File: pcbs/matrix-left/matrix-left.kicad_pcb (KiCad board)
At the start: 2 copper layers, 51 parts, among them J4 Conn_01x11, SW1 SW_Push, SW10 SW_Push, SW11 SW_Push, SW12 SW_Push, SW13 SW_Push, SW14 SW_Push, SW15 SW_Push, SW16 SW_Push, SW17 SW_Push, SW18 SW_Push, SW19 SW_Push, SW2 SW_Push, SW20 SW_Push, SW21 SW_Push, SW22 SW_Push, SW23 SW_Push, SW24 SW_Push, SW25 SW_Push, SW3 SW_Push, SW4 SW_Push, SW5 SW_Push, SW6 SW_Push, SW7 SW_Push, SW8 SW_Push, SW9 SW_Push

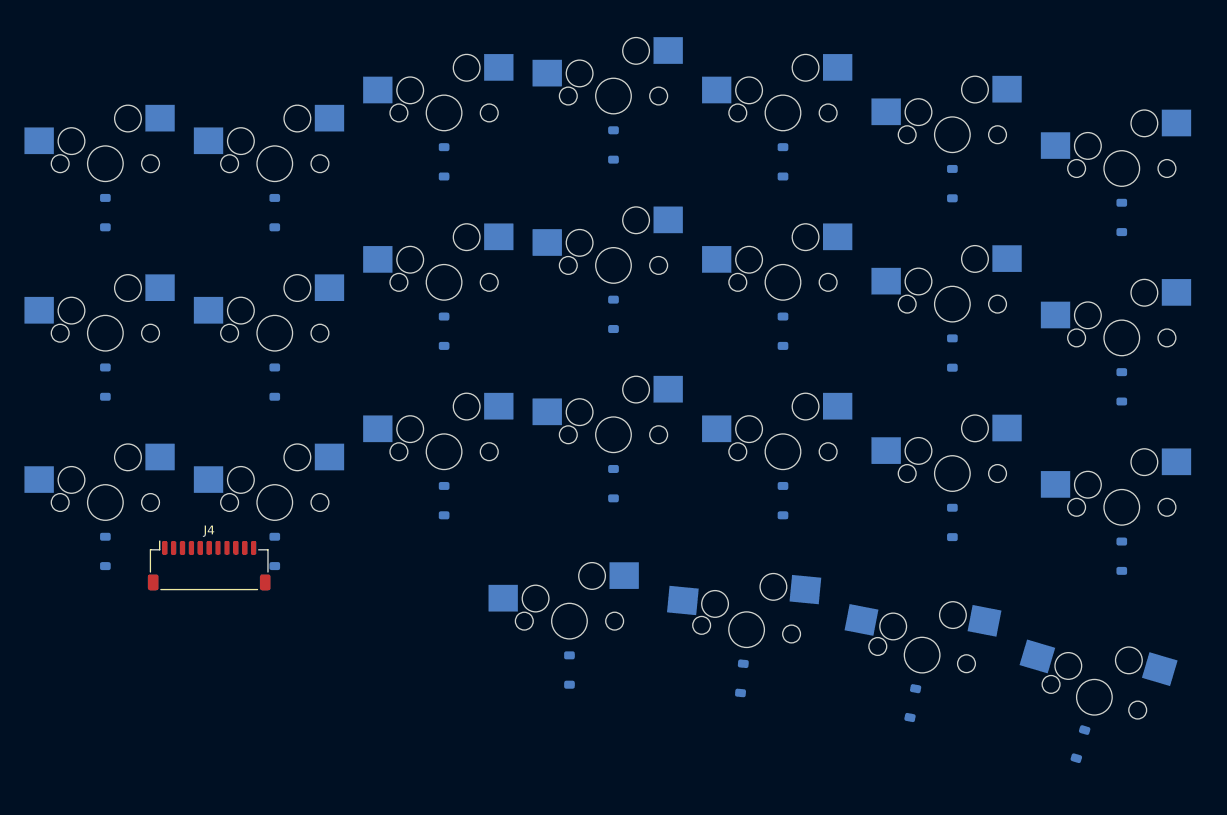
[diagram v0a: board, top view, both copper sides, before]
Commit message: Flip rows R1-R3 on the matrix board and place its J1
All keys in R1-R3 (thumb keys included) are now rotated 180 degrees, so
their hot-swap sockets sit in the front half of the key. R0 keeps its
orientation, which leaves a socket-free band between R0 and R1 across
the board where the column traces can run sideways to J1 at the R0C3 /
R1C3 boundary; below R1 every row gap keeps the usual socket-to-diode
arrangement.

The KiCad board is updated by running place_matrix.py: switches and
diodes placed, diodes on the back, and J1 on the back below R0C3.

Co-Authored-By: Claude Opus 5.5 <noreply@anthropic.com>
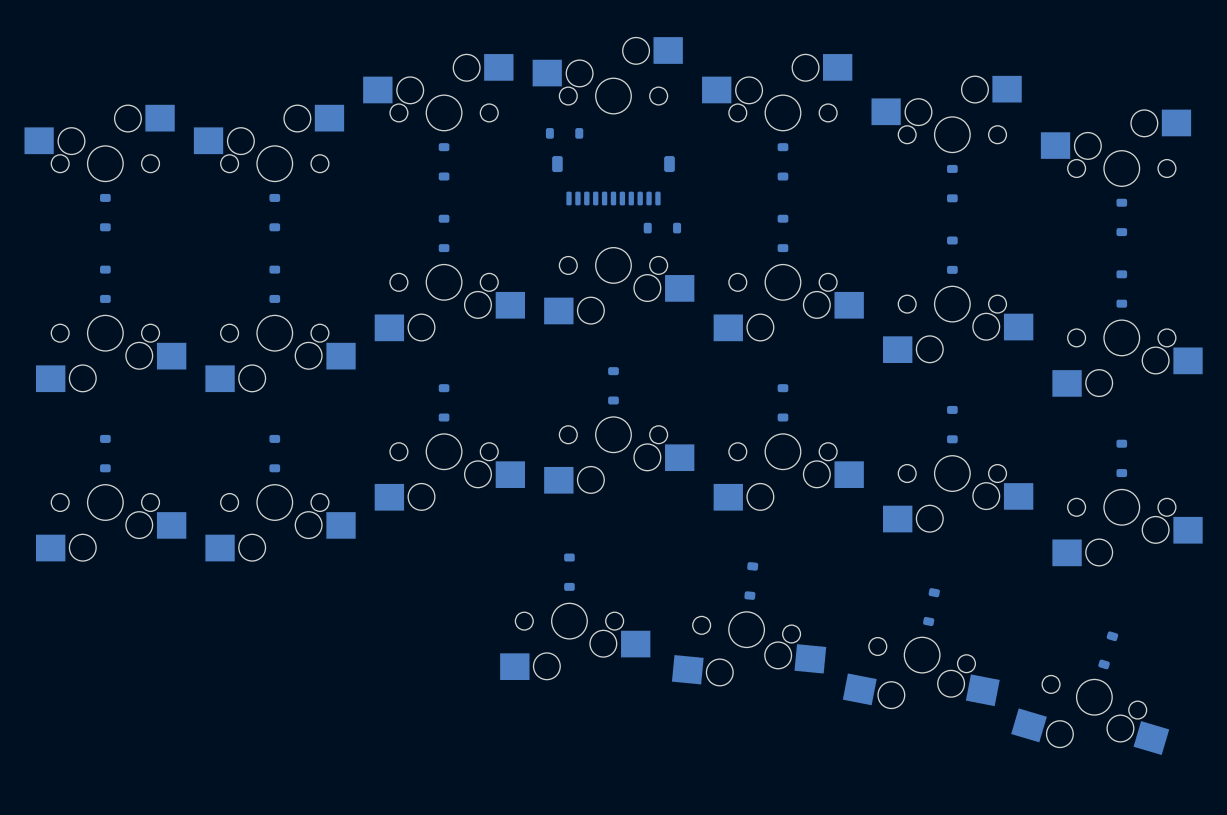
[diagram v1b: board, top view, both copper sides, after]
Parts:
- J4: moved to B.Cu
- moved J4 62.8 mm to (116.7, 69.1)
- moved D11 11.2 mm to (122.2, 74.4), turned to 180 degrees
- moved D23 11.0 mm to (132.2, 114.1)
- moved D10 11.0 mm to (97.6, 75.0)
- moved D12 11.0 mm to (135.7, 75.0)
- moved D13 11.0 mm to (154.8, 77.4)
- moved D14 11.0 mm to (173.8, 81.2)
- moved D15 11.0 mm to (59.5, 99.7)
- moved D16 11.0 mm to (78.6, 99.7)
- moved D17 11.0 mm to (97.6, 94.0)
- moved D18 11.0 mm to (116.7, 92.1)
- moved D19 11.0 mm to (135.7, 94.0)
- moved D20 11.0 mm to (154.8, 96.5)
- moved D21 11.0 mm to (173.8, 100.3)
- moved D22 11.0 mm to (111.7, 113.1)
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
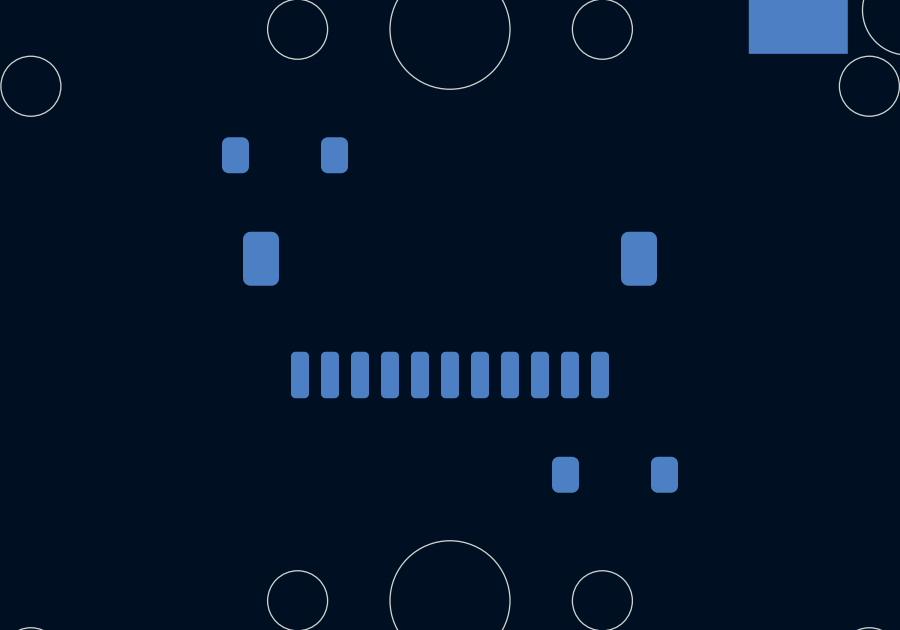
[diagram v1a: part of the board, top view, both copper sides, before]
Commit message: Turn the matrix board J1 so its mouth faces the controller
After flipping a footprint to the back, KiCad stores it as a top-bottom
mirror rotated by 180 degrees, so setting the angle to 0 left J1 mirrored
top to bottom with its mouth facing away from the controller. Add 180
degrees in the placement script, re-run it on the left matrix board, and
match the mock's J1 body to the footprint's fab outline.

Pin 1 (R0) now sits on the +x side, so a straight cable connects
D0-C6 ... D6-C0, D7-R3 ... D10-R0 on both hands.

Co-Authored-By: Claude Opus 5.5 <noreply@anthropic.com>
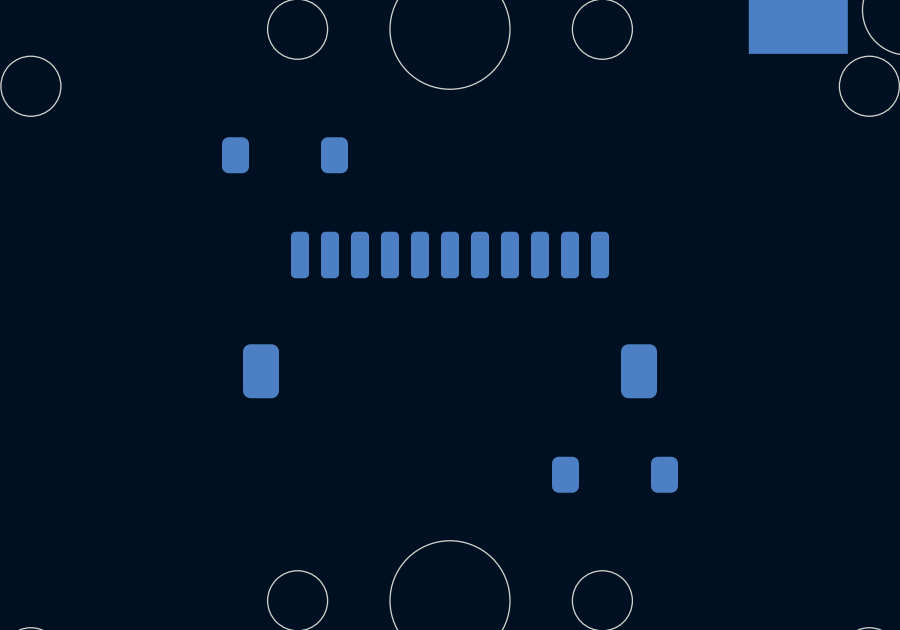
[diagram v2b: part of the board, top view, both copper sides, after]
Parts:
- turned J4 to 180 degrees

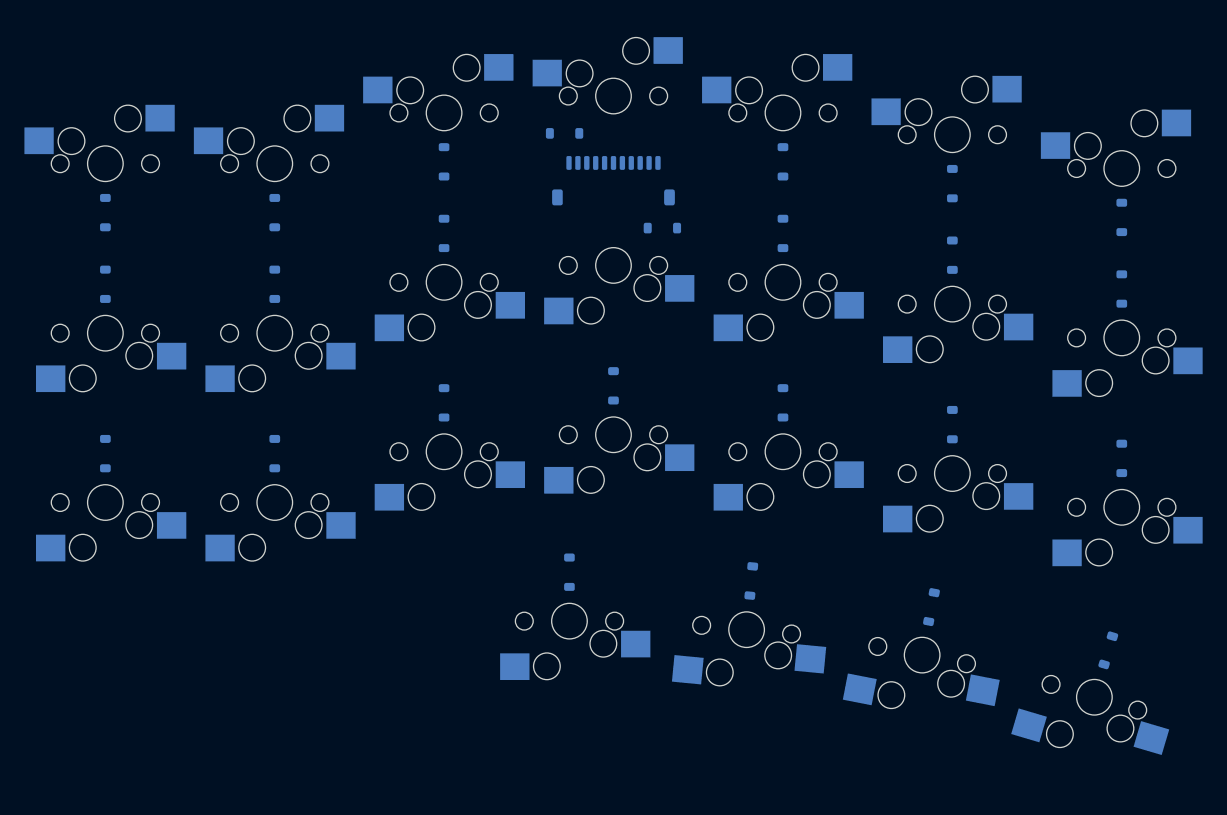
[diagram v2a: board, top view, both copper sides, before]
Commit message: Add the matrix board outline to KiCad and widen it at the sides
The v0.2.0 matrix board had no Edge.Cuts; its outline only existed as
board_outline() in matrix_mock.py. Write it out as JSON and let
scripts/set_edge_cuts.py pick the outline by board file name, then
draw it on the left matrix board.

With the outline inset 0.75 mm all round, the hotswap socket pads of
R0C0 and of the flipped R1-R3 keys in C6 stuck out of the board by
0.33 mm. Keep the 0.75 mm inset on the back and front edges, but grow
the left, right and slanted edges 0.3 mm beyond the plate. Those edges
have no bottom case wall, and the top case's inner face is 0.7 mm out,
so 0.4 mm remains. All pads now keep at least 0.73 mm from the edge and
DRC reports no edge clearance errors.

Co-Authored-By: Claude Opus 5.5 <noreply@anthropic.com>
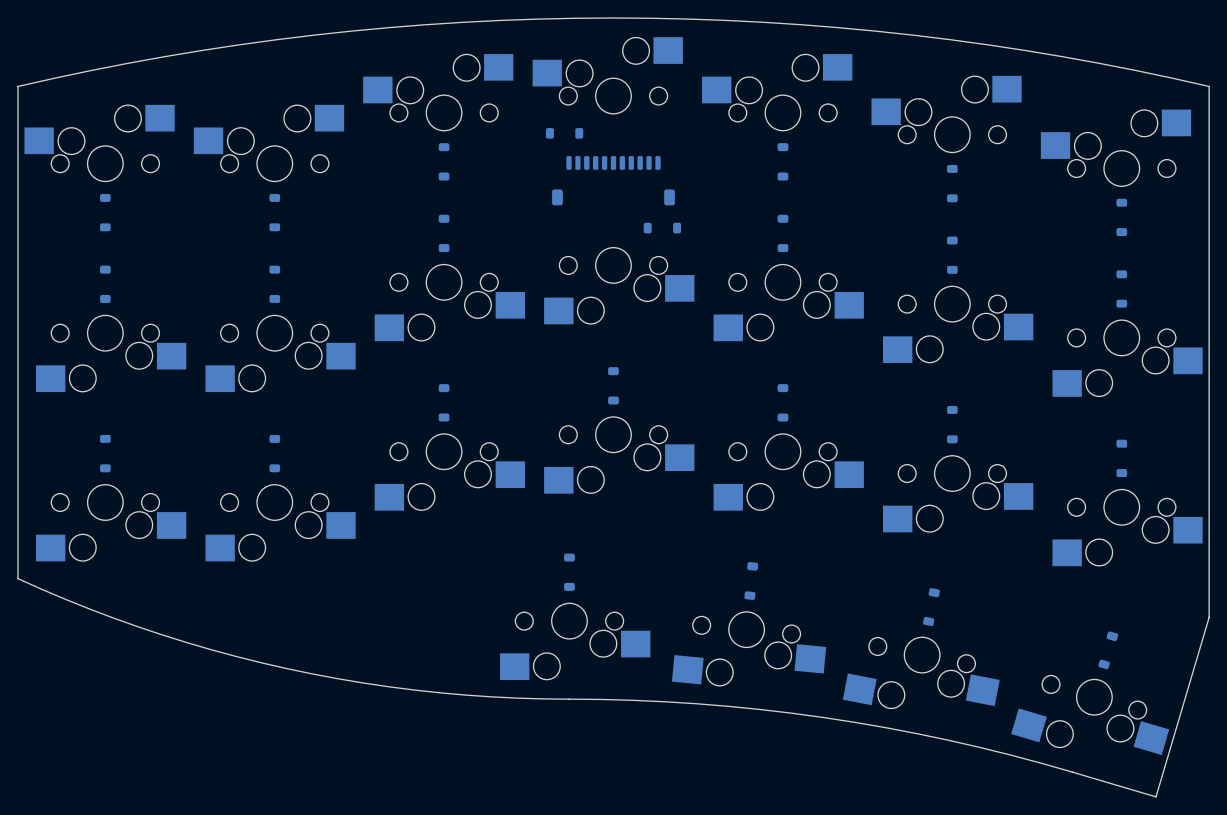
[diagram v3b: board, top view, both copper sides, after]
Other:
- board outline added: 134 x 87.6 mm
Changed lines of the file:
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@@
 		)
+	)
+	(gr_line
+		(start 49.705 58.454598)
+		(end 49.705 113.803738)
+		(stroke
+			(width 0.05)
+			(type default)
+		)
+		(layer "Edge.Cuts")
+	)
+	(gr_arc
+		(start 49.704999 58.454598)
+		(mid 116.679999 50.755)
+		(end 183.654999 58.454598)
+		(stroke
+			(width 0.05)
+			(type default)
+		)
+		(layer "Edge.Cuts")
+	)
+	(gr_arc
+		(start 111.696189 127.355)
+		(mid 79.969078 123.925741)
+		(end 49.704999 113.803738)
+		(stroke
+			(width 0.05)
+			(type default)
+		)
+		(layer "Edge.Cuts")
+	)
+	(gr_arc
+		(start 111.696189 127.355)
+		(mid 140.291304 129.419807)
+		(end 168.294632 135.564532)
+		(stroke
+			(width 0.05)
+			(type default)
+		)
+		(layer "Edge.Cuts")
+	)
+	(gr_line
+		(start 168.294632 135.564532)
+		(end 177.678643 138.344081)
+		(stroke
+			(width 0.05)
+			(type default)
+		)
+		(layer "Edge.Cuts")
+	)
+	(gr_line
+		(start 177.678643 138.344081)
+		(end 183.655 118.166694)
+		(stroke
+			(width 0.05)
+			(type default)
+		)
+		(layer "Edge.Cuts")
+	)
+	(gr_line
+		(start 183.655 118.166694)
+		(end 183.655 58.454598)
+		(stroke
+			(width 0.05)
+			(type default)
+		)
+		(layer "Edge.Cuts")
 	)
 	(embedded_fonts no)

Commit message: Move the matrix board J1 to between R0C4 and R1C4 in KiCad
Re-run the placement script on the left matrix board: J1 (J4) moves to
the C4 band, the C3 diodes go back to their default places and the C4
diodes move aside for J1.

Co-Authored-By: Claude Opus 5.5 <noreply@anthropic.com>
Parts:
- moved J4 19.2 mm to (135.7, 71.0)
- moved D5 5.65 mm to (130.2, 65.6), turned to 0 degrees
- moved D4 5.65 mm to (116.7, 65.0), turned to 90 degrees
- moved D11 5.65 mm to (116.7, 73.1), turned to -90 degrees
- moved D12 5.65 mm to (141.2, 76.3), turned to 180 degrees

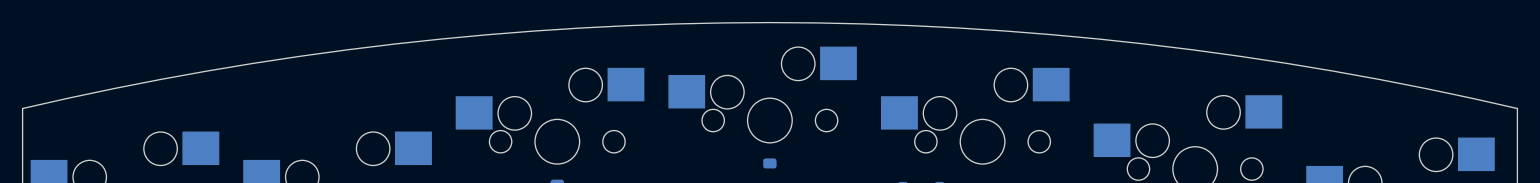
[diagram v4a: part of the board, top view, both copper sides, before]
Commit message: Cut the back screw notches into the left matrix board outline
Redraw Edge.Cuts with set_edge_cuts.py from the outline that
matrix_mock.py writes, which has R4.2 notches around the back screw
bosses. DRC shows no new violations.

Co-Authored-By: Claude Opus 5.5 <noreply@anthropic.com>
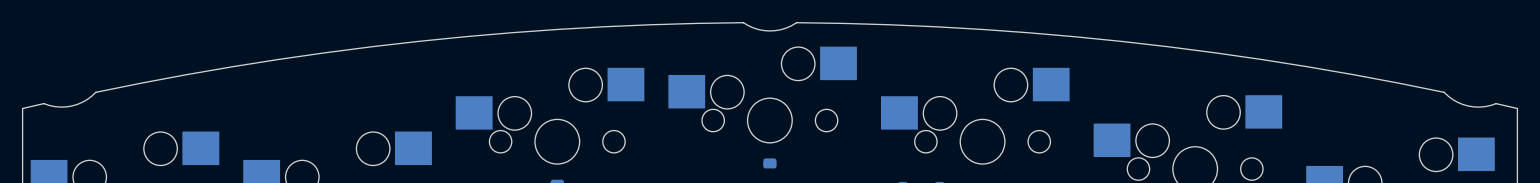
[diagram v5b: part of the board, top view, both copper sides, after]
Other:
- outline, holes or cut-outs redrawn
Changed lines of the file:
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@@
 	(gr_arc
 		(start 49.704999 58.454598)
-		(mid 116.679999 50.755)
-		(end 183.654999 58.454598)
+		(mid 50.658871 58.234009)
+		(end 51.61347 58.016586)
+		(stroke
+			(width 0.05)
+			(type default)
+		)
+		(layer "Edge.Cuts")
+	)
+	(gr_arc
+		(start 56.267428 57.004097)
+		(mid 54.097843 58.233811)
+		(end 51.61347 58.016586)
+		(stroke
+			(width 0.05)
+			(type default)
+		)
+		(layer "Edge.Cuts")
+	)
+	(gr_arc
+		(start 56.267428 57.004097)
+		(mid 85.128393 52.446334)
+		(end 114.298589 50.764607)
 		(stroke
 			(width 0.05)
@@
 		(layer "Edge.Cuts")
 	)
+	(gr_arc
+		(start 119.06141 50.764607)
+		(mid 116.679999 51.505)
+		(end 114.298589 50.764607)
+		(stroke
+			(width 0.05)
+			(type default)
+		)
+		(layer "Edge.Cuts")
+	)
+	(gr_arc
+		(start 119.06141 50.764607)
+		(mid 148.231606 52.446334)
+		(end 177.092571 57.004097)
+		(stroke
+			(width 0.05)
+			(type default)
+		)
+		(layer "Edge.Cuts")
+	)
 	(gr_line
 		(start 168.294632 135.564532)
@@
 		(stroke
 			(width 0.05)
+			(type default)
+		)
+		(layer "Edge.Cuts")
+	)
+	(gr_arc
+		(start 181.746529 58.016586)
+		(mid 179.262156 58.233811)
+		(end 177.092571 57.004097)
+		(stroke
+			(width 0.05)
+			(type default)
+		)
+		(layer "Edge.Cuts")
+	)
+	(gr_arc
+		(start 181.746529 58.016586)
+		(mid 182.701127 58.234009)
+		(end 183.654999 58.454598)
+		(stroke
+			(width 0.05)

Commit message: Route the left matrix board
Update J1 from the schematic, move the diodes and place the column vias
with the scripts, then route: columns on F.Cu, rows and the J1 fan-out
on B.Cu, R2/R3 raised to J1 on F.Cu (36 vias). DRC: no unconnected
items or clearance errors.

Co-Authored-By: Claude Opus 5.5 <noreply@anthropic.com>
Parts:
- moved D12 12.9 mm to (128.4, 77.9), turned to -90 degrees
- moved D5 12.9 mm to (143.0, 64.0), turned to 90 degrees
- moved D7 7.85 mm to (181.1, 70.3)
- moved D24 7.85 mm to (144.7, 118.5)
- moved D25 7.85 mm to (164.5, 122.6)
- moved D20 7.85 mm to (147.5, 99.4)
- moved D14 7.85 mm to (166.5, 84.1)
- moved D23 7.85 mm to (124.6, 116.3)
- moved D17 7.85 mm to (90.3, 96.9)
- moved D10 7.85 mm to (90.3, 77.9)
- moved D13 7.85 mm to (147.5, 80.3)
- moved D6 7.85 mm to (162.1, 66.5)
- moved D15 7.85 mm to (52.2, 102.6)
- moved D8 7.85 mm to (52.2, 83.6)
- moved D1 7.85 mm to (66.8, 69.7)
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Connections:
- J4 pad 1: /R0 -> /C5
- J4 pad 10: /C5 -> /C2
- J4 pad 11: /C6 -> /C3
- J4 pad 2: /R1 -> /C6
- J4 pad 3: /R2 -> /C4
- J4 pad 4: /R3 -> /R0
- J4 pad 5: /C0 -> /R1
- J4 pad 6: /C1 -> /R2
- J4 pad 7: /C2 -> /R3
- J4 pad 8: /C3 -> /C0
- J4 pad 9: /C4 -> /C1
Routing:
- net /R2: track 0.00 -> 146.7 mm, vias 0 -> 2
- net /C0: track 0.00 -> 131.5 mm, vias 0 -> 4
- net /R1: track 0.00 -> 127.5 mm
- net /R0: track 0.00 -> 123.2 mm
- net /C1: track 0.00 -> 111.5 mm, vias 0 -> 4
- net /R3: track 0.00 -> 111.4 mm, vias 0 -> 2
- net /C6: track 0.00 -> 109.0 mm, vias 0 -> 5
- net /C3: track 0.00 -> 90.3 mm, vias 0 -> 5
- net /C5: track 0.00 -> 88.4 mm, vias 0 -> 5
- net /C2: track 0.00 -> 85.7 mm, vias 0 -> 4
- net /C4: track 0.00 -> 81.1 mm, vias 0 -> 5
- net Net-(D21-A): track 0.00 -> 6.49 mm
- net Net-(D17-A): track 0.00 -> 6.49 mm
- net Net-(D20-A): track 0.00 -> 6.49 mm
- net Net-(D16-A): track 0.00 -> 6.49 mm
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
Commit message: Add the name silkscreen and teardrops to the matrix boards
Run add_matrix_silk.py on both boards and add teardrops. Every teardrop
stays at least 0.2 mm from copper on other nets (checked separately,
since DRC does not flag teardrops against other nets' pads). DRC: no
unconnected items or errors.

Co-Authored-By: Claude Opus 5.5 <noreply@anthropic.com>
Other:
- board text added: "optokbd matrix L v0.2.0 2026-10"
